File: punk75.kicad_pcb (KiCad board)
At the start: 2 copper layers, 285.8 x 124.6 mm, 194 parts, among them J1 AVR-ISP-6, SW1 RESET, SW2 BOOT, U1 ATmega32A-PU, Y1 16MHz

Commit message: added gerber files
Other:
- board text added: "JLCJLCJLCJLC"
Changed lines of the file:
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@@
   (general
     (thickness 1.6)
-    (drawings 1169)
+    (drawings 1170)
     (tracks 1702)
     (zones 0)
@@
     (visible_elements FFFFFF7F)
     (pcbplotparams
-      (layerselection 0x010fc_ffffffff)
+      (layerselection 0x010f0_ffffffff)
       (usegerberextensions false)
       (usegerberattributes false)
@@
       (viasonmask false)
       (mode 1)
-      (useauxorigin false)
+      (useauxorigin true)
       (hpglpennumber 1)
       (hpglpenspeed 20)
@@
       (outputformat 1)
       (mirror false)
-      (drillshape 1)
+      (drillshape 0)
       (scaleselection 1)
-      (outputdirectory ""))
+      (outputdirectory "generated/gerber/"))
   )
   (net 0 "")
@@
     )
   )
+  (gr_text JLCJLCJLCJLC (at 98.425 225.933) (layer B.SilkS)
+    (effects (font (size 1 1) (thickness 0.15)) (justify mirror))
+  )
   (gr_line (start 90.551 113.03) (end 89.027 113.937051) (layer F.SilkS) (width 0.3))
   (gr_line (start 230.759 107.696) (end 229.235 108.603051) (layer F.SilkS) (width 0.3))
@@
   (gr_line (start 204.47 173.101) (end 220.853 173.101) (layer B.SilkS) (width 1))
   (gr_line (start 196.342 187.325) (end 204.47 173.101) (layer B.SilkS) (width 1))
-  (gr_text github.com/dsanchezseco/punk75 (at 291.338 208.407) (layer B.SilkS)
+  (gr_text github.com/dsanchezseco/punk75 (at 277.749 207.772) (layer B.SilkS)
     (effects (font (size 2 2) (thickness 0.15)) (justify mirror))
   )

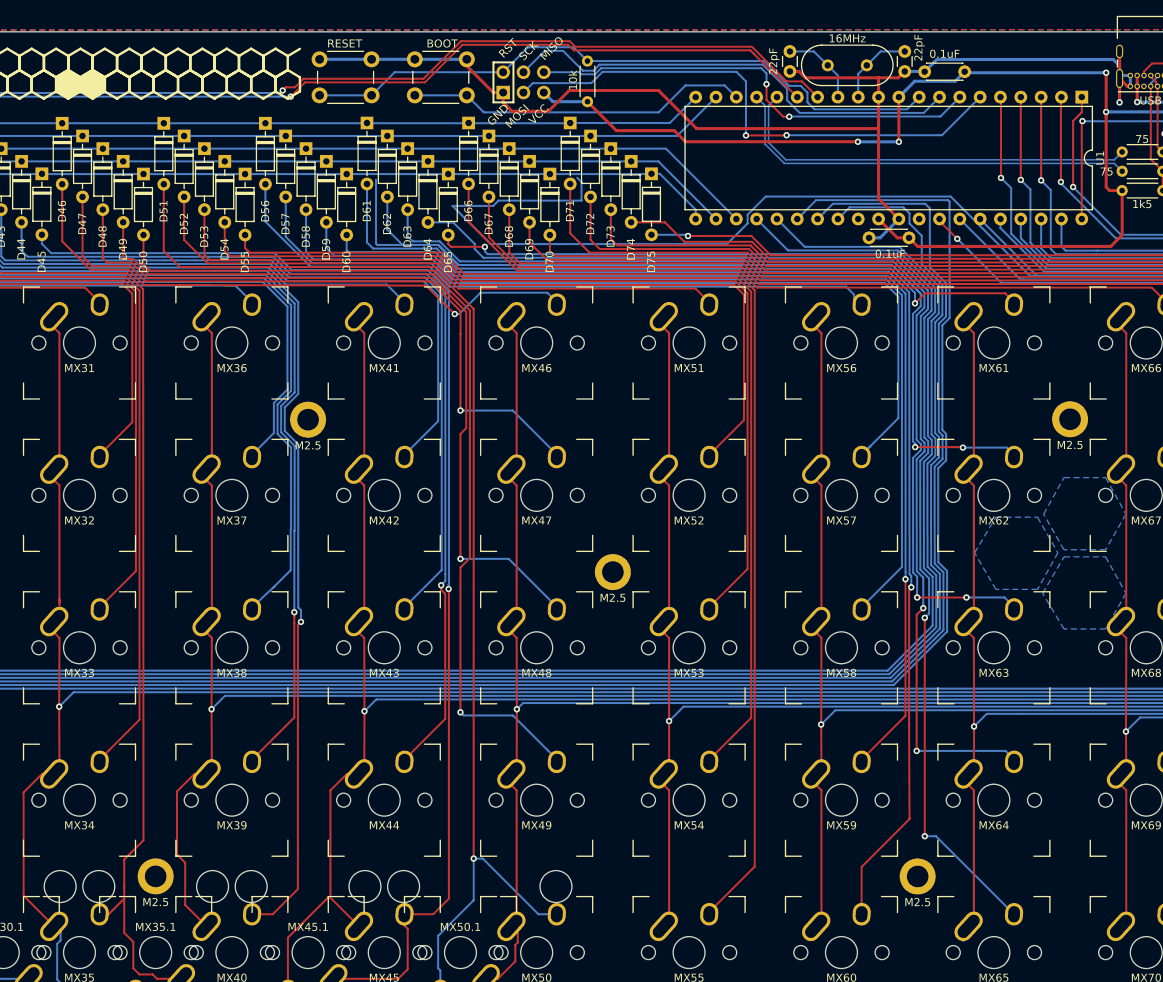
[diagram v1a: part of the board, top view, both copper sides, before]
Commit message: rerouted crystal zone with better shielding
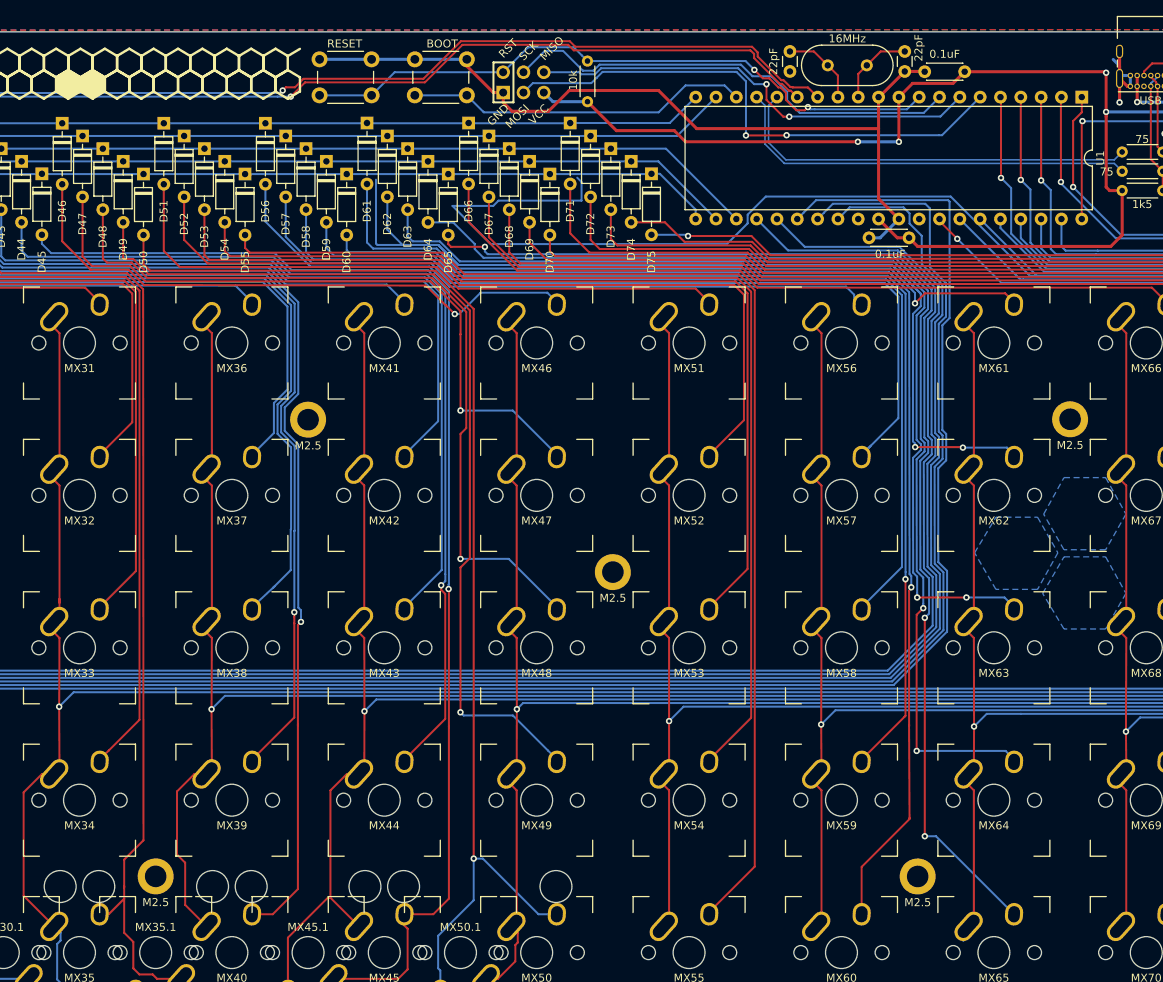
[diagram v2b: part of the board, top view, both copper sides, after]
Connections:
- MX30.1 pad 1: COL5 -> Net-(D30-Pad2)
- MX30.1 pad 2: Net-(D30-Pad2) -> COL5
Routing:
- net GND: track 200.9 -> 163.8 mm
- net COL6: track 331.3 -> 327.6 mm
- net MISO: track 57.9 -> 57.1 mm
- net RESET: track 82.0 -> 82.1 mm, vias 0 -> 2

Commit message: moved holes(again...)
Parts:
- moved H6 38.1 mm to (346.1, 211.1)
- moved H13 38.1 mm to (136.5, 192.1)
- moved H2 38.1 mm to (98.4, 211.1)
- moved H14 38.1 mm to (308.0, 192.1)
- moved RE2 0.12 mm to (353.1, 151.9)
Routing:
- net COL7: track 416.9 -> 295.7 mm
- net COL10: track 229.5 -> 236.6 mm
- net COL9: track 272.9 -> 280.0 mm
- net COL11: track 226.6 -> 232.3 mm
- net Net-(D64-Pad2): track 138.2 -> 134.8 mm
- net R1B: track 262.3 -> 259.2 mm
- net Net-(D65-Pad2): track 149.5 -> 152.0 mm
- net Net-(D60-Pad2): track 155.5 -> 157.9 mm
- net Net-(D15-Pad2): track 96.9 -> 99.1 mm
- net Net-(D70-Pad2): track 169.7 -> 167.7 mm
- net Net-(D5-Pad2): track 90.5 -> 88.7 mm

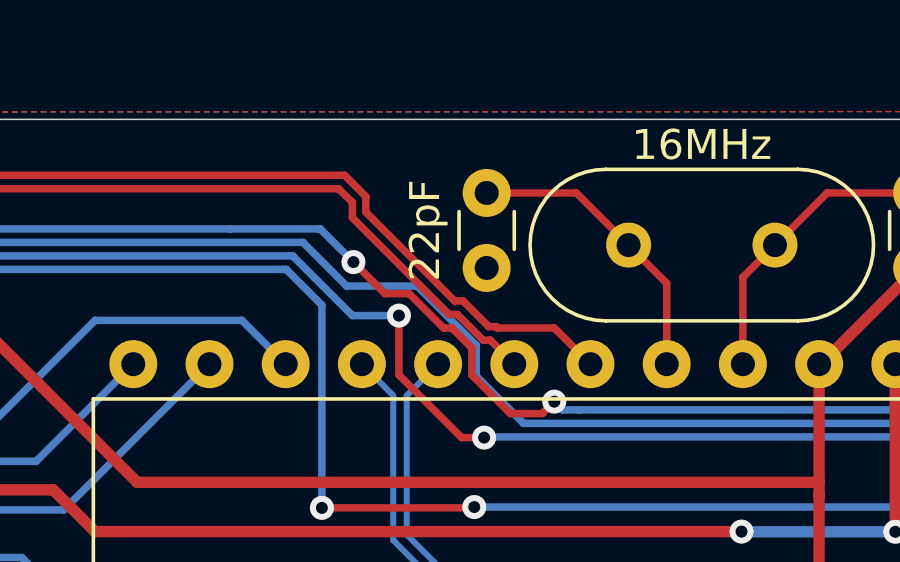
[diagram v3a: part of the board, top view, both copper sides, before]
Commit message: fixed keep-out zone in crystal surroundings
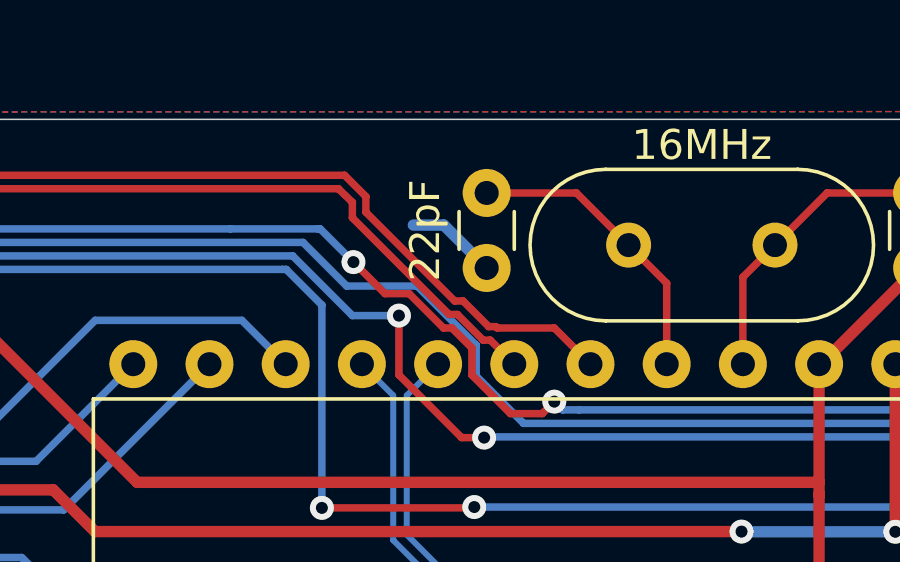
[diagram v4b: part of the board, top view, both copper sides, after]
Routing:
- net GND: track 163.8 -> 166.8 mm
